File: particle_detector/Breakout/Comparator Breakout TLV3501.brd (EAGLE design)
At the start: 21.3 x 17.8 mm, 4 parts

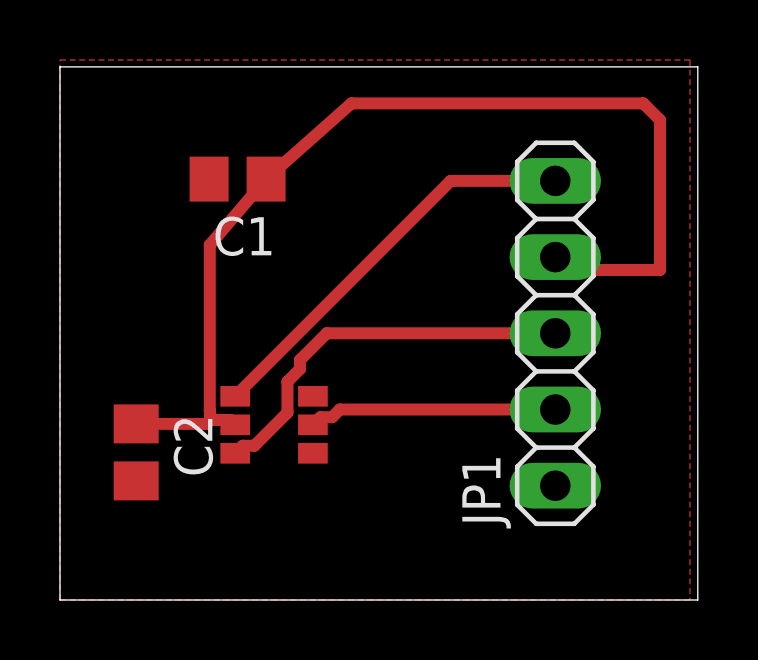
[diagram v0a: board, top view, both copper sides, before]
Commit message: Fixed problematic TLVInsect comparator
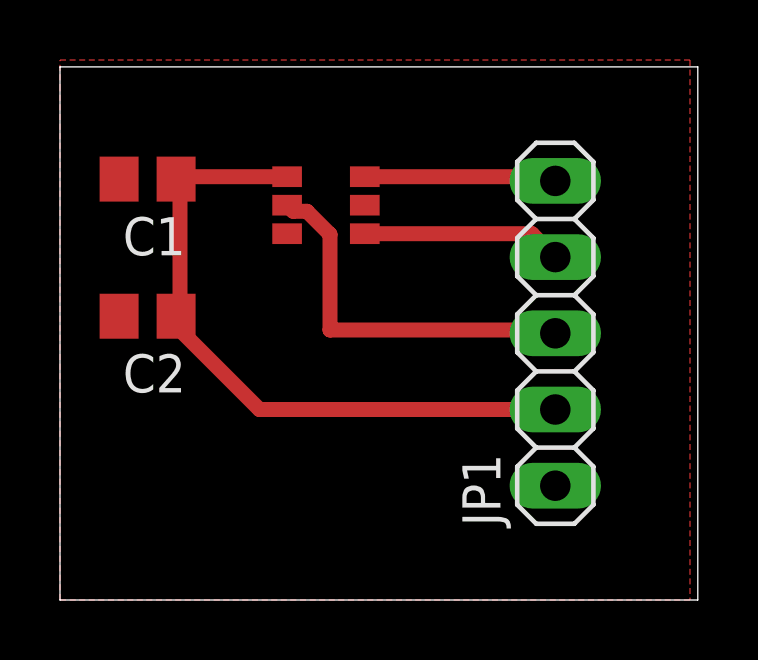
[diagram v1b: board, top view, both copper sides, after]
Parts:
- moved U$1 10.2 mm to (10.2, 14.1), turned to 270 degrees
- moved C2 4.56 mm to (2.92, 9.46), turned to 180 degrees
- moved C1 3.00 mm to (2.92, 14.0)
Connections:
- net 3.3V: now also JP1.2, U$1.P$4; no longer JP1.4, U$1.P$2
- net GND: now also U$1.P$2; no longer U$1.P$4
- net V-: now also JP1.4; no longer JP1.3
- net V0: now also JP1.3; no longer JP1.2
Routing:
- net 3.3V: track 35.1 -> 22.4 mm
- net V+: track 13.6 -> 6.41 mm
- net V-: track 13.1 -> 6.67 mm
- net V0: track 8.29 -> 12.6 mm
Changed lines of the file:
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@@
 <elements>
 <element name="JP1" library="pinhead" library_urn="urn:adsk.eagle:library:325" package="1X05" package3d_urn="urn:adsk.eagle:package:22469/2" value="" x="16.51" y="8.89" rot="R90"/>
-<element name="U$1" library="Personal" package="SOT23-6" value="TLV3501" x="5.84" y="4.89" rot="R90"/>
-<element name="C1" library="rcl" library_urn="urn:adsk.eagle:library:334" package="C0805" package3d_urn="urn:adsk.eagle:package:23617/2" value="" x="5.92" y="14.03" rot="R180">
-<attribute name="SPICEPREFIX" value="C" x="5.92" y="14.03" size="1.778" layer="27" rot="R180" display="off"/>
+<element name="U$1" library="Personal" package="SOT23-6" value="TLV3501" x="10.16" y="14.11" rot="R270"/>
+<element name="C1" library="rcl" library_urn="urn:adsk.eagle:library:334" package="C0805" package3d_urn="urn:adsk.eagle:package:23617/2" value="" x="2.92" y="14.03" rot="R180">
+<attribute name="SPICEPREFIX" value="C" x="2.92" y="14.03" size="1.778" layer="27" rot="R180" display="off"/>
 </element>
-<element name="C2" library="rcl" library_urn="urn:adsk.eagle:library:334" package="C0805" package3d_urn="urn:adsk.eagle:package:23617/2" value="" x="2.54" y="4.92" rot="R270">
-<attribute name="SPICEPREFIX" value="C" x="2.54" y="4.92" size="1.778" layer="27" rot="R270" display="off"/>
+<element name="C2" library="rcl" library_urn="urn:adsk.eagle:library:334" package="C0805" package3d_urn="urn:adsk.eagle:package:23617/2" value="" x="2.92" y="9.46" rot="R180">
+<attribute name="SPICEPREFIX" value="C" x="2.92" y="9.46" size="1.778" layer="27" rot="R180" display="off"/>
 </element>
 </elements>
@@
 <signal name="V-">
 <contactref element="U$1" pad="P$1"/>
-<contactref element="JP1" pad="3"/>
-<wire x1="5.84" y1="4.89" x2="6.0926" y2="5.1426" width="0.4" layer="1"/>
-<wire x1="6.0926" y1="5.1426" x2="6.48096875" y2="5.1426" width="0.4" layer="1"/>
-<wire x1="8" y1="7.69836875" x2="8" y2="8" width="0.4" layer="1"/>
-<wire x1="7.5826" y1="7.28096875" x2="8" y2="7.69836875" width="0.4" layer="1"/>
-<wire x1="6.48096875" y1="5.1426" x2="7.5826" y2="6.24423125" width="0.4" layer="1"/>
-<wire x1="7.5826" y1="6.24423125" x2="7.5826" y2="7.28096875" width="0.4" layer="1"/>
-<wire x1="8" y1="8" x2="8.89" y2="8.89" width="0.4" layer="1"/>
-<wire x1="8.89" y1="8.89" x2="16.51" y2="8.89" width="0.4" layer="1"/>
+<contactref element="JP1" pad="4"/>
+<wire x1="10.16" y1="12.21" x2="15.73" y2="12.21" width="0.5" layer="1"/>
+<wire x1="15.73" y1="12.21" x2="16.51" y2="11.43" width="0.5" layer="1"/>
 </signal>
 <signal name="V0">
 <contactref element="U$1" pad="P$5"/>
-<contactref element="JP1" pad="2"/>
-<wire x1="8.43" y1="5.84" x2="8.6826" y2="6.0926" width="0.4" layer="1"/>
-<wire x1="8.6826" y1="6.0926" x2="9.07096875" y2="6.0926" width="0.4" layer="1"/>
-<wire x1="9.32836875" y1="6.35" x2="16.51" y2="6.35" width="0.4" layer="1"/>
-<wire x1="9.07096875" y1="6.0926" x2="9.32836875" y2="6.35" width="0.4" layer="1"/>
+<contactref element="JP1" pad="3"/>
+<wire x1="7.57" y1="13.16" x2="7.7726" y2="12.9574" width="0.5" layer="1"/>
+<wire x1="7.7726" y1="12.9574" x2="8.23168125" y2="12.9574" width="0.5" layer="1"/>
+<wire x1="8.23168125" y1="12.9574" x2="9" y2="12.18908125" width="0.5" layer="1"/>
+<wire x1="9" y1="12.18908125" x2="9" y2="9" width="0.5" layer="1"/>
+<wire x1="9" y1="9" x2="16.4" y2="9" width="0.5" layer="1"/>
+<wire x1="16.4" y1="9" x2="16.51" y2="8.89" width="0.5" layer="1"/>
 </signal>
 <signal name="V+">
 <contactref element="U$1" pad="P$3"/>
 <contactref element="JP1" pad="5"/>
-<wire x1="5.84" y1="6.79" x2="13.02" y2="13.97" width="0.4" layer="1"/>
-<wire x1="13.02" y1="13.97" x2="16.51" y2="13.97" width="0.4" layer="1"/>
+<wire x1="10.16" y1="14.11" x2="16.37" y2="14.11" width="0.5" layer="1"/>
+<wire x1="16.37" y1="14.11" x2="16.51" y2="13.97" width="0.5" layer="1"/>
 </signal>
 <signal name="3.3V">
-<contactref element="JP1" pad="4"/>
-<contactref element="U$1" pad="P$2"/>
 <contactref element="C1" pad="1"/>
 <contactref element="C2" pad="1"/>
-<wire x1="5.84" y1="5.84" x2="5.68" y2="6" width="0.4" layer="1"/>
-<wire x1="5.68" y1="6" x2="5" y2="6" width="0.4" layer="1"/>
-<wire x1="5" y1="6" x2="5" y2="6.29163125" width="0.4" layer="1"/>
-<wire x1="5" y1="6.29163125" x2="4.9926" y2="6.29903125" width="0.4" layer="1"/>
-<wire x1="4.9926" y1="6.29903125" x2="4.9926" y2="11.8326" width="0.4" layer="1"/>
-<wire x1="4.9926" y1="11.8326" x2="6.87" y2="14.03" width="0.4" layer="1"/>
-<wire x1="6.87" y1="14.03" x2="9.714" y2="16.554" width="0.4" layer="1"/>
-<wire x1="19.446" y1="16.554" x2="20" y2="16" width="0.4" layer="1"/>
-<wire x1="20" y1="16" x2="20" y2="11" width="0.4" layer="1"/>
-<wire x1="20" y1="11" x2="16.94" y2="11" width="0.4" layer="1"/>
-<wire x1="16.94" y1="11" x2="16.51" y2="11.43" width="0.4" layer="1"/>
-<wire x1="9.714" y1="16.554" x2="19.446" y2="16.554" width="0.4" layer="1"/>
-<wire x1="2.54" y1="5.87" x2="4.87" y2="5.87" width="0.4" layer="1"/>
-<wire x1="4.87" y1="5.87" x2="5" y2="6" width="0.4" layer="1"/>
+<contactref element="U$1" pad="P$4"/>
+<contactref element="JP1" pad="2"/>
+<wire x1="7.57" y1="14.11" x2="3.95" y2="14.11" width="0.5" layer="1"/>
+<wire x1="3.95" y1="14.11" x2="3.87" y2="14.03" width="0.5" layer="1"/>
+<wire x1="3.87" y1="14.03" x2="4" y2="13.9" width="0.5" layer="1"/>
+<wire x1="4" y1="13.9" x2="4" y2="9" width="0.5" layer="1"/>
+<wire x1="4" y1="9" x2="6.65" y2="6.35" width="0.5" layer="1"/>
+<wire x1="6.65" y1="6.35" x2="16.51" y2="6.35" width="0.5" layer="1"/>
+<wire x1="4" y1="9" x2="3.87" y2="9.46" width="0" layer="19" extent="1-1"/>
 </signal>
 <signal name="GND" airwireshidden="yes">
-<contactref element="U$1" pad="P$4"/>
 <contactref element="U$1" pad="P$6"/>
 <contactref element="C1" pad="2"/>
 <contactref element="C2" pad="2"/>
 <contactref element="JP1" pad="1"/>
-<wire x1="8.32" y1="5" x2="8.43" y2="4.89" width="0.4" layer="1"/>
-<wire x1="2.54" y1="3.97163125" x2="2.54" y2="3.97" width="0.4" layer="1"/>
 <polygon width="0.4" layer="1">
 <vertex x="0" y="17"/>
@@
 <vertex x="0" y="0"/>
 </polygon>
-<wire x1="8.32" y1="5" x2="8.43" y2="6.79" width="0" layer="19" extent="1-1"/>
+<contactref element="U$1" pad="P$2"/>
 </signal>
 </signals>
